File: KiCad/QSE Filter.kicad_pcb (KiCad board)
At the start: 2 copper layers, 65.2 x 74.5 mm, 66 parts, among them J1 RF In, J2 RF Out, J3 Power, J4 Control In, Q1 2N7002, Q2 2N7002, Q4 2N7002, Q5 2N7002, U1 EB2-12NU, U2 EB2-12NU, U4 EB2-12NU, U5 EB2-12NU

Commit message: Created project symbol and footprint libraries
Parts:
- C1, C10, C11, C12, C13, C14, C15, C16, C17, C18, C19, C2, C20, C23, C24, C25, C26, C27, C28, C29, C3, C30, C31, C32, C33, C34, C35, C36, C4, C5, C6, C7, C8, C9: footprint Capacitor_SMD:C_0805_2012Metric -> QSE Filter:C_0805_2012Metric
- D1, D2, D4, D5: footprint Diode_SMD:D_SOD-323 -> QSE Filter:D_SOD-323
- J1, J2: footprint DigiKey:CONN_RF2-04A-T-00-50-G_ADM -> QSE Filter:CONN_RF2-04A-T-00-50-G_ADM
- J3: footprint Connector_IDC:IDC-Header_2x08_P2.54mm_Vertical -> QSE Filter:IDC-Header_2x08_P2.54mm_Vertical
- J4: footprint Connector_IDC:IDC-Header_2x05_P2.54mm_Vertical -> QSE Filter:IDC-Header_2x05_P2.54mm_Vertical
- L1, L10, L2, L3, L4, L5, L7, L8, L9: footprint DigiKey:IND_1008CS_COC -> QSE Filter:IND_1008CS_COC
- L6: footprint DigiKey:INDC2015X152N -> QSE Filter:INDC2015X152N
- Q1, Q2, Q4, Q5: footprint Package_TO_SOT_SMD:SOT-23 -> QSE Filter:SOT-23
- R1, R2, R3, R4: footprint Resistor_SMD:R_0805_2012Metric -> QSE Filter:R_0805_2012Metric
- REF** (x2): footprint MountingHole:MountingHole_3.2mm_M3 -> QSE Filter:MountingHole_3.2mm_M3
- U1, U2, U4, U5: footprint DigiKey:EB2-12NU_KEM -> QSE Filter:EB2-12NU_KEM

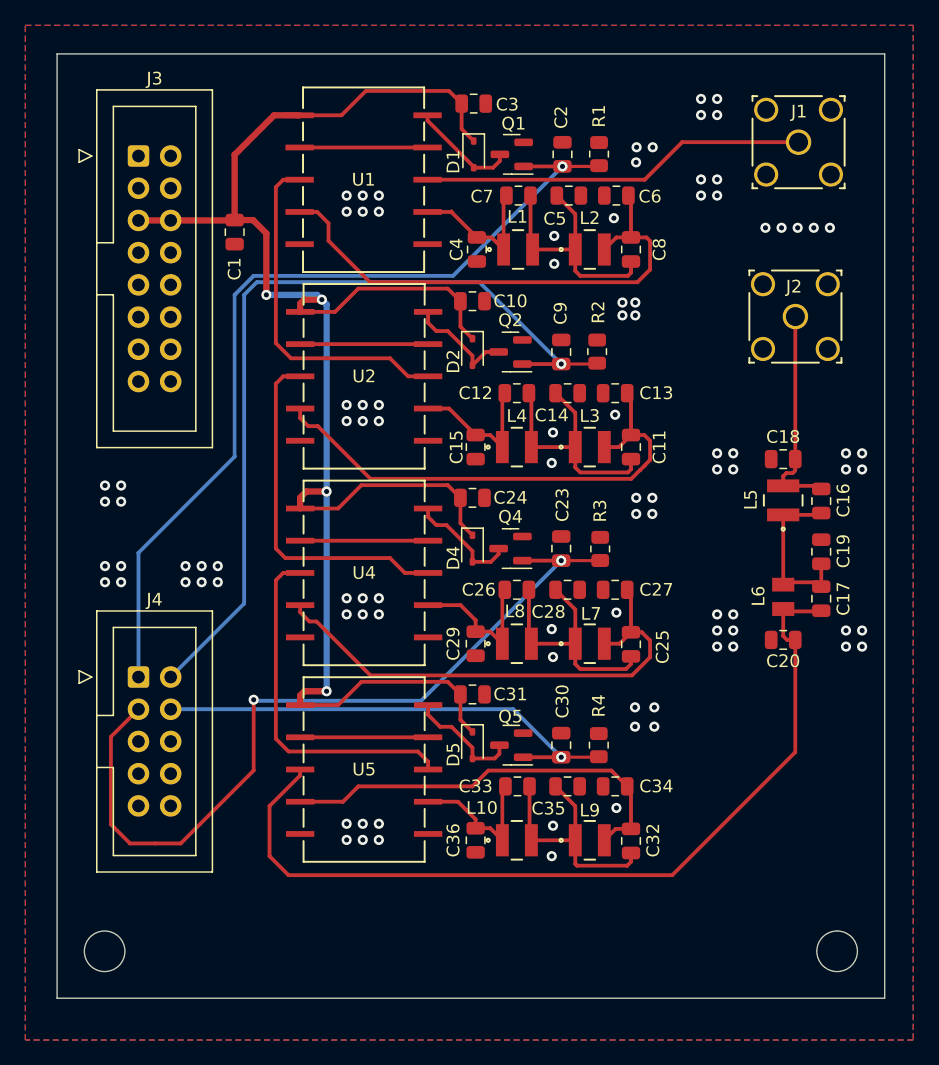
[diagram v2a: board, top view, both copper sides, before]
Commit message: Initial layout with switched 10m LPF.  Passes all DRC however has some islands and has a trace possibly too close to the edge of the PCB.
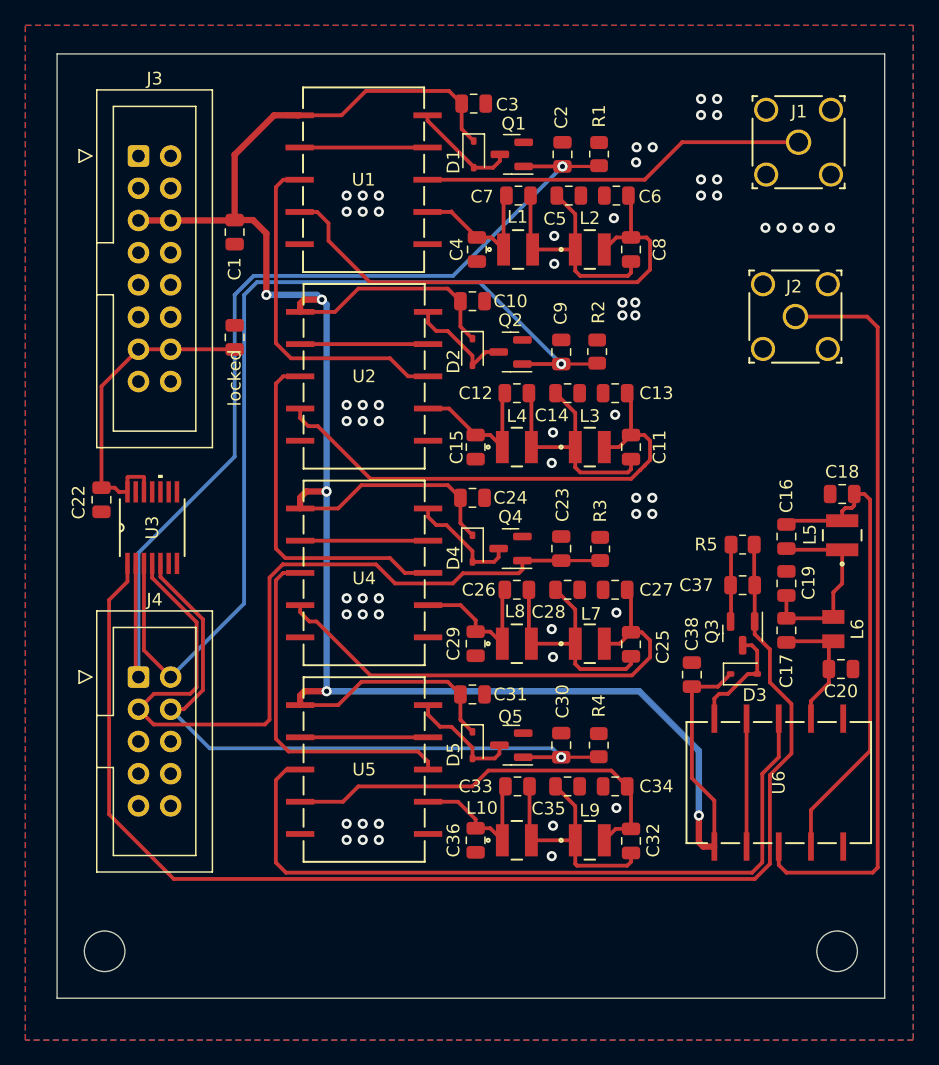
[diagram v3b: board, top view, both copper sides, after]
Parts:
- added C22: 0.1uF, QSE Filter:C_0805_2012Metric, F.Cu at (81.0, 82.4)
- added C37: 0.1uF, QSE Filter:C_0805_2012Metric, F.Cu at (131.6, 89.1)
- added C38: 0.1uF, QSE Filter:C_0805_2012Metric, F.Cu at (127.5, 96.2)
- added D3: 1N4148WS, QSE Filter:D_SOD-323, F.Cu at (131.7, 96.1)
- added Q3: 2N7002, QSE Filter:SOT-23, F.Cu at (131.6, 92.9)
- added R5: 6.8K, QSE Filter:R_0805_2012Metric, F.Cu at (131.6, 85.9)
- added U3: CD74HC4002PWR, QSE Filter:PW14, F.Cu at (85.0, 84.6)
- added U6: EB2-12NU, QSE Filter:EB2-12NU_KEM, F.Cu at (134.4, 104.7)
- added locked: 0.1uF, QSE Filter:C_0805_2012Metric, F.Cu at (91.5, 69.6)
- moved C18 5.40 mm to (139.4, 82.0)
- moved L5 5.40 mm to (139.4, 85.2)
- moved C20 5.10 mm to (139.3, 95.8), turned to 0 degrees
- moved L6 4.70 mm to (138.7, 92.6)
- moved C16 3.92 mm to (135.0, 85.3)
- moved C17 3.72 mm to (135.0, 92.7)
- moved C19 3.72 mm to (135.0, 89.0)
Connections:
- C16 pad 2: RF_Out -> Net-(C16-Pad2)
- C17 pad 1: 15M_Out -> Net-(C17-Pad1)
- C18 pad 1: RF_Out -> Net-(C16-Pad2)
- C20 pad 1: 15M_Out -> Net-(C17-Pad1)
- J3 pad 13: unconnected-(J3-Pin_13-Pad13) -> +3.3V
- J3 pad 14: unconnected-(J3-Pin_14-Pad14) -> +3.3V
- L5 pad 2: RF_Out -> Net-(C16-Pad2)
- L6 pad 1: 15M_Out -> Net-(C17-Pad1)
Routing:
- net Band_10M: track 0.00 -> 102.2 mm
- net +12V: track 140.1 -> 196.7 mm, vias 4 -> 5
- net RF_Out: track 17.1 -> 59.1 mm
- net Net-(C16-Pad2): track 0.00 -> 38.4 mm
- net +3.3V: track 0.00 -> 25.5 mm
- net Band_15M: track 38.4 -> 52.9 mm
- net Net-(C17-Pad1): track 0.00 -> 10.6 mm
- net Net-(U6-Pad2): track 0.00 -> 10.1 mm
- net Band_40M: track 66.6 -> 76.4 mm
- net 15M_Out: track 69.0 -> 59.7 mm
- net Band_80M: track 69.3 -> 78.4 mm
- net Net-(D3-A): track 0.00 -> 8.93 mm
- net GND: track 0.00 -> 6.08 mm, vias 96 -> 60
- net Net-(C16-Pad1): track 13.3 -> 15.6 mm
- net Band_20M: track 64.8 -> 67.0 mm, vias 2 -> 0

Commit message: Resolved ground pour islands, moved RF out trace off the extreme right edge of the PCB, other minor layout changes.
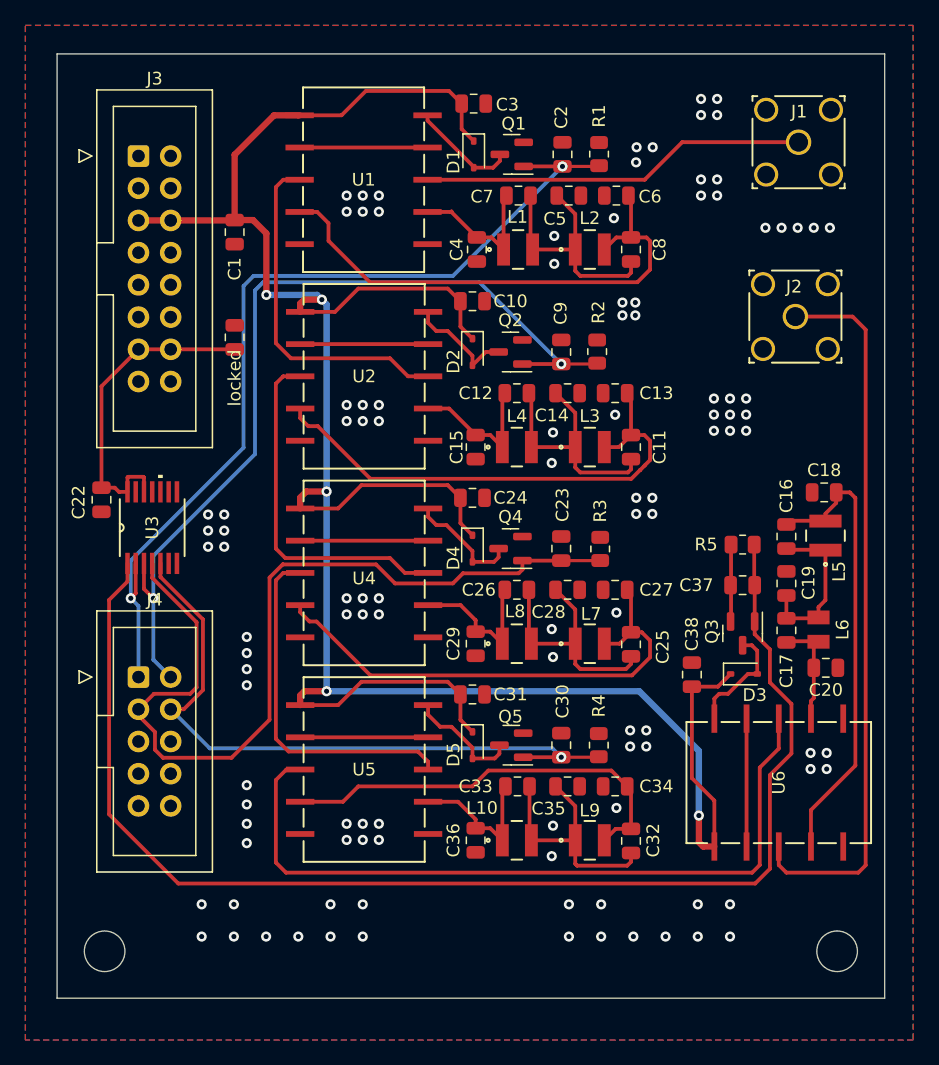
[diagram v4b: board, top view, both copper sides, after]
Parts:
- moved C18 1.43 mm to (138.0, 81.8)
- moved L5 1.32 mm to (138.1, 85.2)
- moved C20 1.19 mm to (138.1, 95.7)
- moved L6 1.17 mm to (137.5, 92.6)
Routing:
- net Band_40M: track 76.4 -> 70.5 mm, vias 1 -> 2
- net Band_80M: track 78.4 -> 73.1 mm, vias 1 -> 2
- net Band_20M: track 67.0 -> 70.3 mm
- net Net-(C16-Pad1): track 15.6 -> 13.0 mm
- net RF_Out: track 59.1 -> 57.0 mm
- net Net-(C17-Pad1): track 10.6 -> 8.89 mm
- net Band_10M: track 102.2 -> 102.7 mm
- net GND: vias 60 -> 111
